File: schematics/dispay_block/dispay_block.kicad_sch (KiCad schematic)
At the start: 5 parts

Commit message: hw: annotate schematics and add capacitor footprints
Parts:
- added C2: 0.1uF, Capacitor_SMD:C_0201_0603Metric, symbol Device:C
- C1: renamed from C?; value C -> 0.1uF; footprint (none) -> Capacitor_SMD:C_0201_0603Metric
- gave numbers to parts that had none: 4
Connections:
- net +5V: now also U2.16 (VCC), C2.2
- net GND: now also C2.1

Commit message: hw: add display segment schematic and PCB v1
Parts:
- removed J1: Conn_01x21_Pin, Connector_PinHeader_1.00mm:PinHeader_1x21_P1.00mm_Horizontal, symbol Connector:Conn_01x21_Pin
- removed J2: Conn_01x21_Socket, Connector_PinHeader_1.00mm:PinHeader_1x21_P1.00mm_Horizontal, symbol Connector:Conn_01x21_Socket
- removed U1, U2: 74HC595, Package_SO:SOIC-16_3.9x9.9mm_P1.27mm, symbol 74xx:74HC595
- added H1, H2, H3, H4: MountingHole, MountingHole:MountingHole_3.2mm_M3, symbol Mechanical:MountingHole
- added J1, J2: Conn_02x10_Odd_Even, Connector_PinSocket_2.54mm:PinSocket_2x10_P2.54mm_Vertical, symbol Connector_Generic:Conn_02x10_Odd_Even
- added J3: Conn_02x01, Connector_PinHeader_2.54mm:PinHeader_2x01_P2.54mm_Vertical, symbol Connector_Generic:Conn_02x01
- added Q1, Q2, Q3, Q4, Q5, Q6, Q7, Q8: BC847BS, Package_TO_SOT_SMD:SOT-363_SC-70-6, symbol Transistor_BJT:BC847BS
- added R1, R10, R11, R12, R14, R15, R2, R3, R4, R5, R6, R7, R8, R9: 270, Resistor_SMD:R_0603_1608Metric, symbol Device:R
- added R13, R16: 33K, Resistor_SMD:R_0603_1608Metric, symbol Device:R
- added TP1: RESET, TestPoint:TestPoint_Pad_D2.0mm, symbol Connector:TestPoint_Small
- added TP2: TestPoint, TestPoint:TestPoint_Pad_D2.0mm, symbol Connector:TestPoint
- added U1: CH32V003FxUx, Package_DFN_QFN:QFN-20-1EP_3x3mm_P0.4mm_EP1.65x1.65mm, symbol MCU_WCH_CH32V0:CH32V003FxUx
- C1: footprint Capacitor_SMD:C_0201_0603Metric -> Capacitor_SMD:C_0603_1608Metric
- C2: value 0.1uF -> 1uF; footprint Capacitor_SMD:C_0201_0603Metric -> Capacitor_SMD:C_0603_1608Metric
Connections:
- net GND: now also J2.1 (Pin_1), J2.2 (Pin_2), J3.2 (Pin_2), Q1.1 (E1), Q1.4 (E2), Q2.1 (E1), Q2.4 (E2), Q3.1 (E1), Q3.4 (E2), Q4.1 (E1), Q4.4 (E2), Q5.1 (E1), Q5.4 (E2), Q6.1 (E1), Q6.4 (E2), Q7.1 (E1), Q7.4 (E2), Q8.1 (E1), Q8.4 (E2), U1.21 (VSS), U1.4 (VSS)
- net +5V renamed +3V3
- net +3V3: now also J2.7 (Pin_7), J2.8 (Pin_8), U1.6 (VDD)
- new net: Q7.5 (B2), R13.2
- new net: Q4.5 (B2), R7.2
- new net: R1.1, U1.16 (PD2)
- new net: Q1.2 (B1), R1.2
- new net: Q1.5 (B2), R2.2
- new net: R15.1, U1.5 (PD0)
- new net: Q8.2 (B1), R15.2
- new net: R3.1, U1.14 (PC7)
- new net: Q2.2 (B1), R3.2
- new net: R7.1, U1.17 (PD3)
- new net: Q6.2 (B1), R11.2
- new net: Q6.5 (B2), R12.2
- new net: R9.1, TP2.1, U1.10 (PC3)
- new net: R14.1, TP1.1, U1.1 (PD7)
- new net: R11.1, U1.19 (PD5)
- new net: Q5.2 (B1), R5.2
- new net: R5.1, U1.11 (PC4)
- new net: R6.1, U1.12 (PC5)
- new net: R4.1, U1.13 (PC6)
- new net: R8.1, U1.18 (PD4)
- new net: R13.1, U1.2 (PA1)
- new net: R12.1, U1.20 (PD6)
- new net: R16.1, U1.3 (PA2)
- new net: R10.1, U1.7 (PC0)
- new net: Q3.5 (B2), R10.2
- new net: Q2.5 (B2), R4.2
- new net: Q7.2 (B1), R14.2
- new net: Q5.5 (B2), R6.2
- new net: Q4.2 (B1), R8.2
- new net: Q8.5 (B2), R16.2
- new net: Q3.2 (B1), R9.2
- new net A_1: J1.1 (Pin_1), J1.2 (Pin_2)
- new net A_2: J1.3 (Pin_3), J1.4 (Pin_4)
- new net A_3: J1.5 (Pin_5), J1.6 (Pin_6)
- new net A_4: J1.7 (Pin_7), J1.8 (Pin_8)
- new net A_5: J1.10 (Pin_10), J1.9 (Pin_9)
- new net A_6: J1.11 (Pin_11), J1.12 (Pin_12)
- new net A_7: J1.13 (Pin_13), J1.14 (Pin_14)
- new net A_8: J1.15 (Pin_15), J1.16 (Pin_16)
- new net B_1: J1.17 (Pin_17), J1.18 (Pin_18)
- new net B_2: J1.19 (Pin_19), J1.20 (Pin_20)
- new net B_3: J2.10 (Pin_10), J2.9 (Pin_9)
- new net B_4: J2.11 (Pin_11), J2.12 (Pin_12)
- new net B_5: J2.13 (Pin_13), J2.14 (Pin_14)
- new net B_6: J2.15 (Pin_15), J2.16 (Pin_16)
- new net B_7: J2.17 (Pin_17), J2.18 (Pin_18)
- new net B_8: J2.19 (Pin_19), J2.20 (Pin_20)
- new net CC1: Q1.3 (C2)
- new net CC10: Q7.3 (C2)
- new net CC11: Q7.6 (C1)
- new net CC12: Q3.3 (C2)
- new net CC13: Q6.3 (C2)
- new net CC14: Q6.6 (C1)
- new net CC15: Q8.3 (C2)
- new net CC16: Q8.6 (C1)
- new net CC2: Q1.6 (C1)
- new net CC3: Q5.3 (C2)
- new net CC4: Q5.6 (C1)
- new net CC5: Q4.6 (C1)
- new net CC6: Q2.3 (C2)
- new net CC7: Q2.6 (C1)
- new net CC8: Q3.6 (C1)
- new net CC9: Q4.3 (C2)
- new net SCL: J2.3 (Pin_3), J2.4 (Pin_4), U1.9 (PC2)
- new net SDA: J2.5 (Pin_5), J2.6 (Pin_6), U1.8 (PC1)
- new net SWIO: J3.1 (Pin_1), R2.1, U1.15 (PD1)
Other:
- company: (none) -> Author: Kacper Jelonek

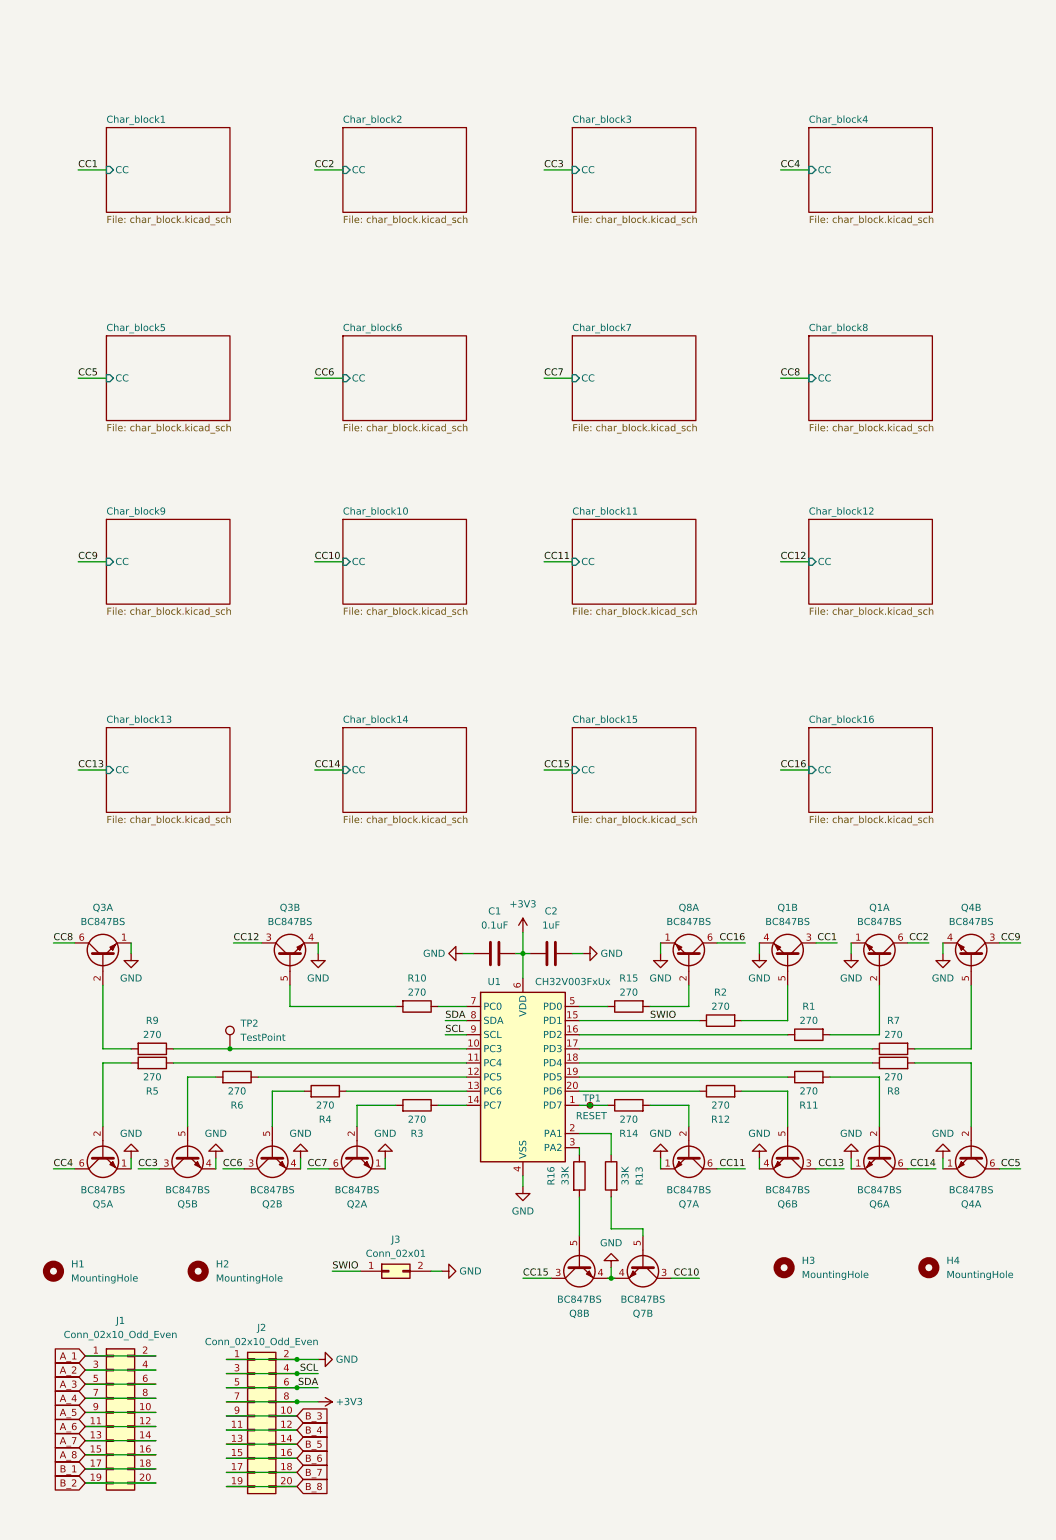
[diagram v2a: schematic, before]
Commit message: hw: revise display design and fix wrong footprint
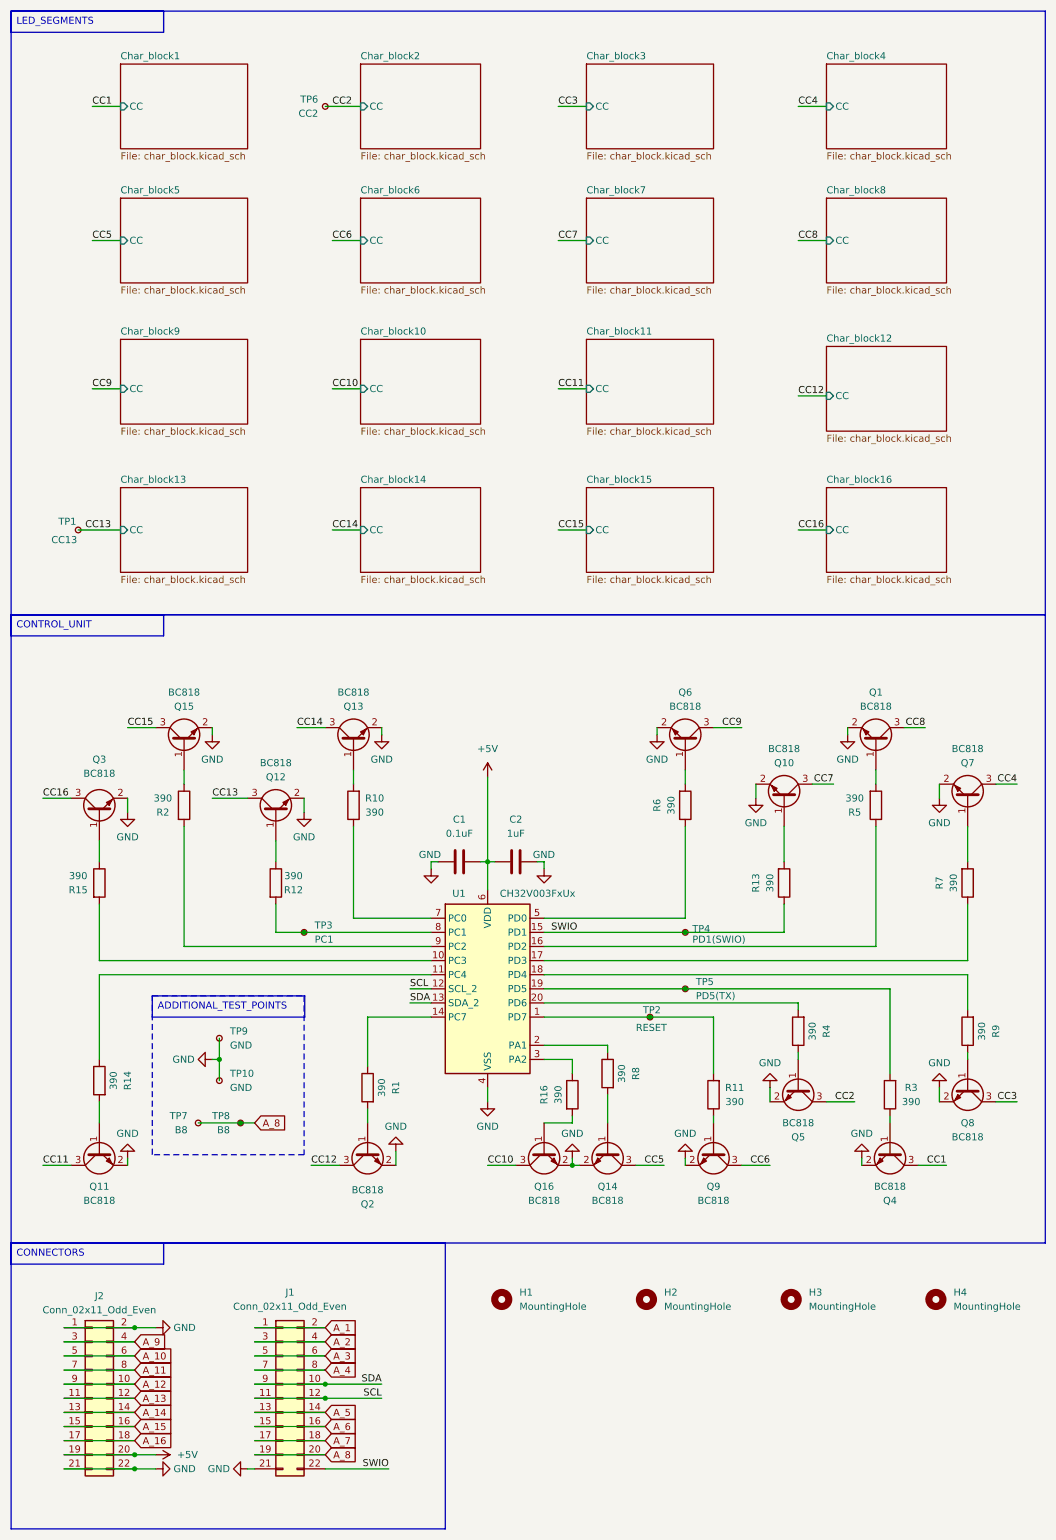
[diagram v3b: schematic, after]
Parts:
- removed J1, J2: Conn_02x10_Odd_Even, Connector_PinSocket_2.54mm:PinSocket_2x10_P2.54mm_Vertical, symbol Connector_Generic:Conn_02x10_Odd_Even
- removed J3: Conn_02x01, Connector_PinHeader_2.54mm:PinHeader_2x01_P2.54mm_Vertical, symbol Connector_Generic:Conn_02x01
- removed Q1, Q2, Q3, Q4, Q5, Q6, Q7, Q8: BC847BS, Package_TO_SOT_SMD:SOT-363_SC-70-6, symbol Transistor_BJT:BC847BS
- removed TP2: TestPoint, TestPoint:TestPoint_Pad_D2.0mm, symbol Connector:TestPoint
- added J1, J2: Conn_02x11_Odd_Even, Connector_PinHeader_2.54mm:PinHeader_2x11_P2.54mm_Vertical, symbol Connector_Generic:Conn_02x11_Odd_Even
- added Q1, Q10, Q11, Q12, Q13, Q14, Q15, Q16, Q2, Q3, Q4, Q5, Q6, Q7, Q8, Q9: BC818, Package_TO_SOT_SMD:SOT-23, symbol Transistor_BJT:BC818
- added TP1: CC13, TestPoint:TestPoint_Pad_D1.5mm, symbol Connector:TestPoint_Small
- added TP10, TP9: GND, TestPoint:TestPoint_Pad_D1.0mm, symbol Connector:TestPoint_Small
- added TP3: PC1, TestPoint:TestPoint_Pad_D1.5mm, symbol Connector:TestPoint_Small
- added TP4: PD1(SWIO), TestPoint:TestPoint_Pad_D1.5mm, symbol Connector:TestPoint_Small
- added TP5: PD5(TX), TestPoint:TestPoint_Pad_D1.5mm, symbol Connector:TestPoint_Small
- added TP6: CC2, TestPoint:TestPoint_Pad_D1.5mm, symbol Connector:TestPoint_Small
- added TP7, TP8: B8, TestPoint:TestPoint_Pad_D1.5mm, symbol Connector:TestPoint_Small
- R1: renamed from R10; value 270 -> 390
- R10: renamed from R11; value 270 -> 390
- R11: renamed from R4; value 270 -> 390
- R12, R14, R8: value 270 -> 390
- R13: renamed from R3; value 270 -> 390
- R15: renamed from R16; value 33K -> 390
- R16: renamed from R13; value 33K -> 390
- R2: renamed from R15; value 270 -> 390
- R3: renamed from R2; value 270 -> 390
- R4: renamed from R1; value 270 -> 390
- R5: renamed from R9; value 270 -> 390
- R6: renamed from R7; value 270 -> 390
- R7: renamed from R5; value 270 -> 390
- R9: renamed from R6; value 270 -> 390
- TP2: renamed from TP1; footprint TestPoint:TestPoint_Pad_D2.0mm -> TestPoint:TestPoint_Pad_D1.5mm
- renumbered H3 to H1, H4 to H2, H1 to H3, H2 to H4
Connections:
- net A_1: now also J1.1 (Pin_1), J1.2 (Pin_2)
- net A_2: now also J1.3 (Pin_3), J1.4 (Pin_4)
- net A_3: now also J1.5 (Pin_5), J1.6 (Pin_6)
- net A_4: now also J1.7 (Pin_7), J1.8 (Pin_8)
- net A_5: now also J1.13 (Pin_13), J1.14 (Pin_14)
- net A_6: now also J1.15 (Pin_15), J1.16 (Pin_16)
- net A_7: now also J1.17 (Pin_17), J1.18 (Pin_18)
- net A_8: now also J1.19 (Pin_19), J1.20 (Pin_20), TP7.1, TP8.1
- net CC1: now also Q4.3 (C)
- net CC10: now also Q16.3 (C)
- net CC11: now also Q11.3 (C)
- net CC12: now also Q2.3 (C)
- net CC13: now also Q12.3 (C), TP1.1
- net CC14: now also Q13.3 (C)
- net CC15: now also Q15.3 (C)
- net CC16: now also Q3.3 (C)
- net CC2: now also Q5.3 (C), TP6.1
- net CC3: now also Q8.3 (C)
- net CC4: now also Q7.3 (C)
- net CC5: now also Q14.3 (C)
- net CC6: now also Q9.3 (C)
- net CC7: now also Q10.3 (C)
- net CC8: now also Q1.3 (C)
- net CC9: now also Q6.3 (C)
- net GND: now also J1.21 (Pin_21), J2.1 (Pin_1), J2.2 (Pin_2), J2.21 (Pin_21), J2.22 (Pin_22), Q1.2 (E), Q10.2 (E), Q11.2 (E), Q12.2 (E), Q13.2 (E), Q14.2 (E), Q15.2 (E), Q16.2 (E), Q2.2 (E), Q3.2 (E), Q4.2 (E), Q5.2 (E), Q6.2 (E), Q7.2 (E), Q8.2 (E), Q9.2 (E), TP10.1, TP9.1
- net SCL: now also U1.12 (PC5), J1.11 (Pin_11), J1.12 (Pin_12); no longer U1.9 (PC2)
- net SDA: now also U1.13 (PC6), J1.10 (Pin_10), J1.9 (Pin_9); no longer U1.8 (PC1)
- net SWIO: now also R13.1, J1.22 (Pin_22), TP4.1; no longer R3.1
- net at R16.2: now also Q16.1 (B)
- net at R6.2: now also Q6.1 (B)
- net at R4.1: now also Q5.1 (B); no longer U1.16 (PD2)
- net at R4.2: now also U1.20 (PD6)
- net at R3.2: now also U1.19 (PD5), TP5.1
- net at R2.1: now also Q15.1 (B); no longer U1.5 (PD0)
- net at R2.2: now also U1.9 (PC2)
- net at U1.14 (PC7): now also R1.1; no longer R13.1
- net at R13.2: now also Q10.1 (B)
- net at R6.1: now also U1.5 (PD0); no longer U1.17 (PD3)
- net at R10.2: now also Q13.1 (B)
- net at R12.2: now also U1.8 (PC1), TP3.1
- net at U1.10 (PC3): now also R15.2; no longer R5.1
- net at TP2.1, U1.1 (PD7): now also R11.2; no longer R14.1
- net at R10.1: now also U1.7 (PC0); no longer U1.19 (PD5)
- net at R7.2: now also Q7.1 (B)
- net at R7.1: now also U1.17 (PD3); no longer U1.11 (PC4)
- net at R9.1: now also Q8.1 (B); no longer U1.12 (PC5)
- net at R11.1: now also Q9.1 (B); no longer U1.13 (PC6)
- net at U1.18 (PD4): now also R9.2; no longer R8.1
- net at U1.2 (PA1): now also R8.1; no longer R16.1
- net at R12.1: now also Q12.1 (B); no longer U1.20 (PD6)
- net at R15.1: now also Q3.1 (B); no longer U1.3 (PA2)
- net at R1.2: now also Q2.1 (B)
- net at R14.2: now also Q11.1 (B)
- net at R8.2: now also Q14.1 (B)
- net at R5.2: now also Q1.1 (B)
- net +3V3 renamed +5V
- net +5V: now also J2.19 (Pin_19), J2.20 (Pin_20)
- new net: Q4.1 (B), R3.1
- new net: R14.1, U1.11 (PC4)
- new net: R5.1, U1.16 (PD2)
- new net: R16.1, U1.3 (PA2)
- new net A_10: J2.5 (Pin_5), J2.6 (Pin_6)
- new net A_11: J2.7 (Pin_7), J2.8 (Pin_8)
- new net A_12: J2.10 (Pin_10), J2.9 (Pin_9)
- new net A_13: J2.11 (Pin_11), J2.12 (Pin_12)
- new net A_14: J2.13 (Pin_13), J2.14 (Pin_14)
- new net A_15: J2.15 (Pin_15), J2.16 (Pin_16)
- new net A_16: J2.17 (Pin_17), J2.18 (Pin_18)
- new net A_9: J2.3 (Pin_3), J2.4 (Pin_4)
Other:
- title: Display Block -> DISPLAY_SEGMENT
- moved on the sheet: C1, C2, H1, H2, H3, H4, R1, R10, R11, R12, R13, R14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
